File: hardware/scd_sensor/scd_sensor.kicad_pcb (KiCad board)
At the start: 2 copper layers, 18.6 x 27.4 mm, 2 parts, among them J5 Conn_02x10_Odd_Even, U1 SCD41-D-R2

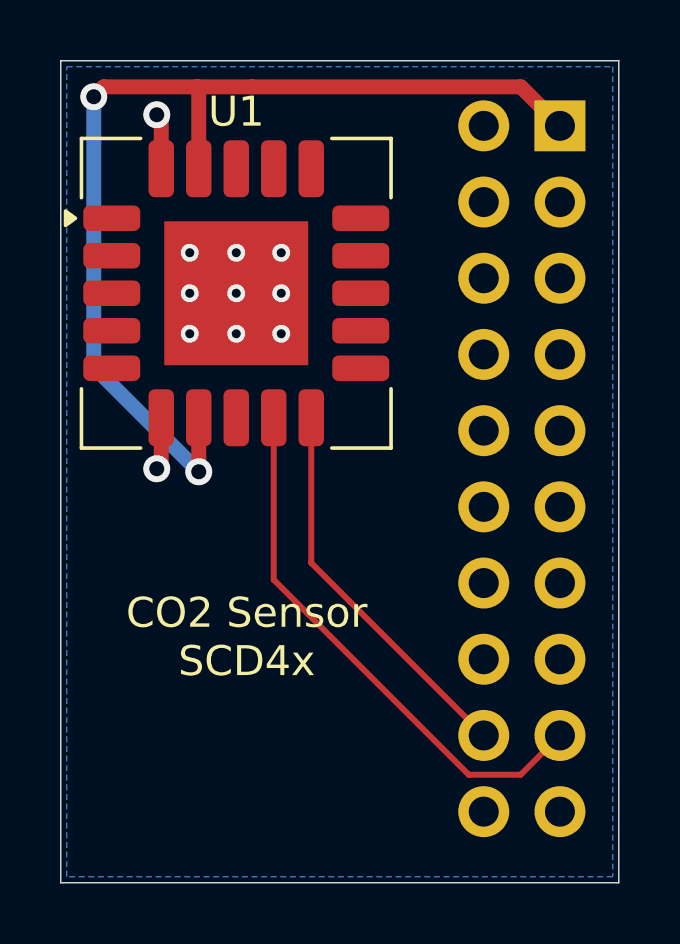
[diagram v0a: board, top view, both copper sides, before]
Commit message: Add sensor board
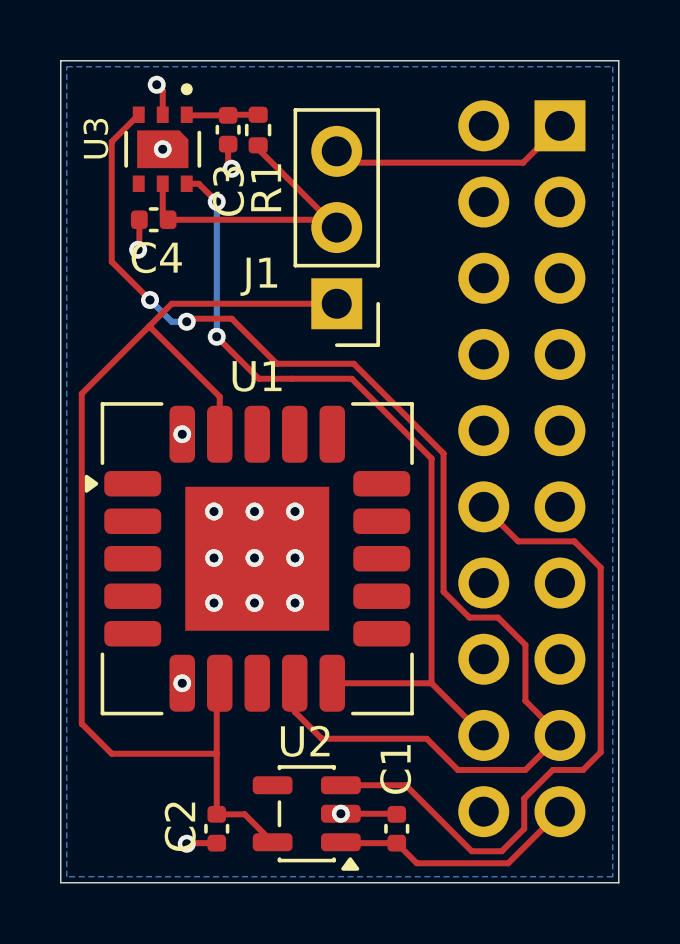
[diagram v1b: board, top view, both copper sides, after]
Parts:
- added C1: 1u, Capacitor_SMD:C_0402_1005Metric, F.Cu at (141.0, 118.0)
- added C2: 4u7, Capacitor_SMD:C_0402_1005Metric, F.Cu at (135.0, 118.0)
- added C3: 1u, Capacitor_SMD:C_0402_1005Metric, F.Cu at (135.4, 94.7)
- added C4: 1u, Capacitor_SMD:C_0402_1005Metric, F.Cu at (132.9, 97.7)
- added J1: Conn_01x03, Connector_PinHeader_2.54mm:PinHeader_1x03_P2.54mm_Vertical, F.Cu at (139.0, 100.5)
- added R1: 4R7, Resistor_SMD:R_0402_1005Metric, F.Cu at (136.4, 94.7)
- added U2: TPS76333, Package_TO_SOT_SMD:SOT-23-5, F.Cu at (138.0, 117.5)
- added U3: SGP40-D-R4, Project_Footprints:XCDR_SGP40-D-R4, F.Cu at (133.2, 95.3)
- moved U1 8.88 mm to (136.3, 109.0)
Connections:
- J5 pad 12: unconnected-(J5-Pin_12-Pad12) -> /PB0
- J5 pad 19: GND -> /SYS
- U1 pad 19: /3V3 -> Net-(J1-Pin_1)
- U1 pad 7: /3V3 -> Net-(J1-Pin_1)
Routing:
- net Net-(J1-Pin_1): track 0.00 -> 36.9 mm
- net /3V3: track 34.7 -> 7.57 mm, vias 2 -> 0
- net /SCL: track 18.2 -> 41.7 mm, vias 0 -> 2
- net /PB0: track 0.00 -> 22.4 mm
- net /SDA: track 13.0 -> 27.9 mm, vias 0 -> 2
- net Net-(J1-Pin_2): track 0.00 -> 10.3 mm
- net /SYS: track 0.00 -> 8.26 mm
- net Net-(U3-VDD): track 0.00 -> 2.34 mm
- net GND: track 3.62 -> 5.85 mm, vias 11 -> 17
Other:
- board text added: "CO2 Sensor"
- board text added: "SCD4x"
- board text added: "SGP40"
- board text removed: "CO2 Sensor SCD4x"
